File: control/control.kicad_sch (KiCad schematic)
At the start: 51 parts, among them J1 Conn_01x02_Pin, J3 Conn_01x02_Pin, J4 Conn_01x07_Pin, J9 Conn_01x04_Male, P1 Conn_01x03_Pin, P2 Conn_01x03_Pin, P3 Conn_01x03_Pin, P4 Conn_01x03_Pin, SW1 SW_Push, U1 STM32F103C8Tx, Y1 8Mhz

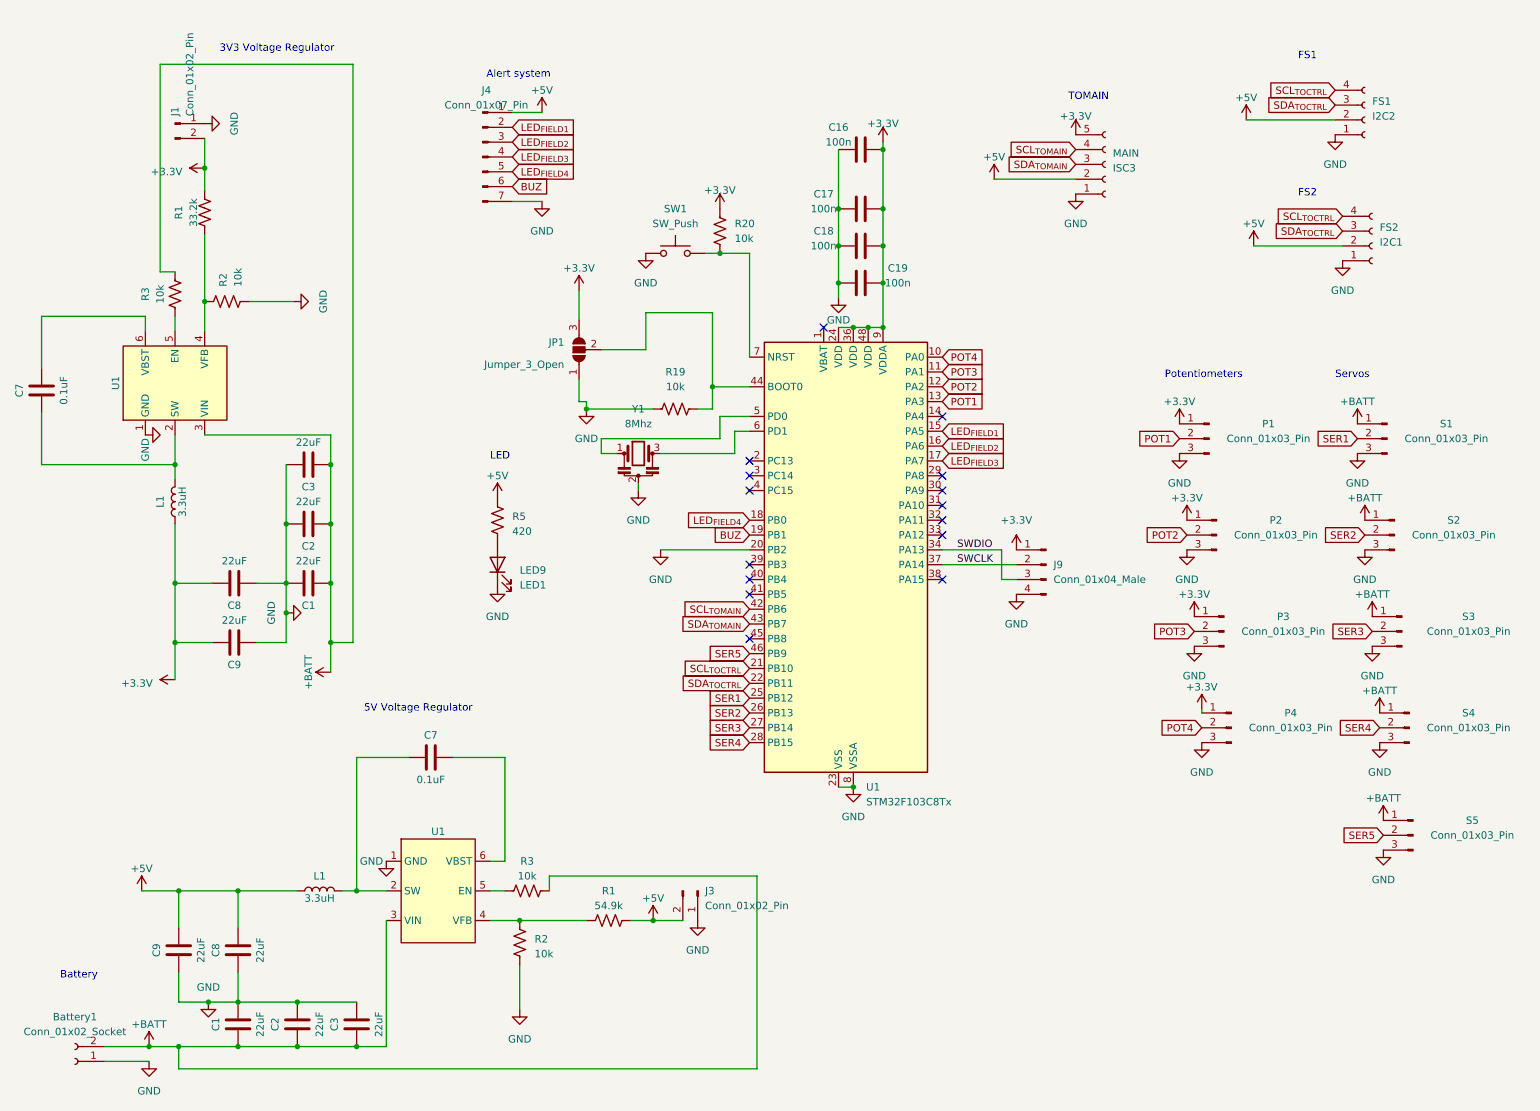
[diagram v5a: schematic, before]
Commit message: increased size and updated silkscreen labels
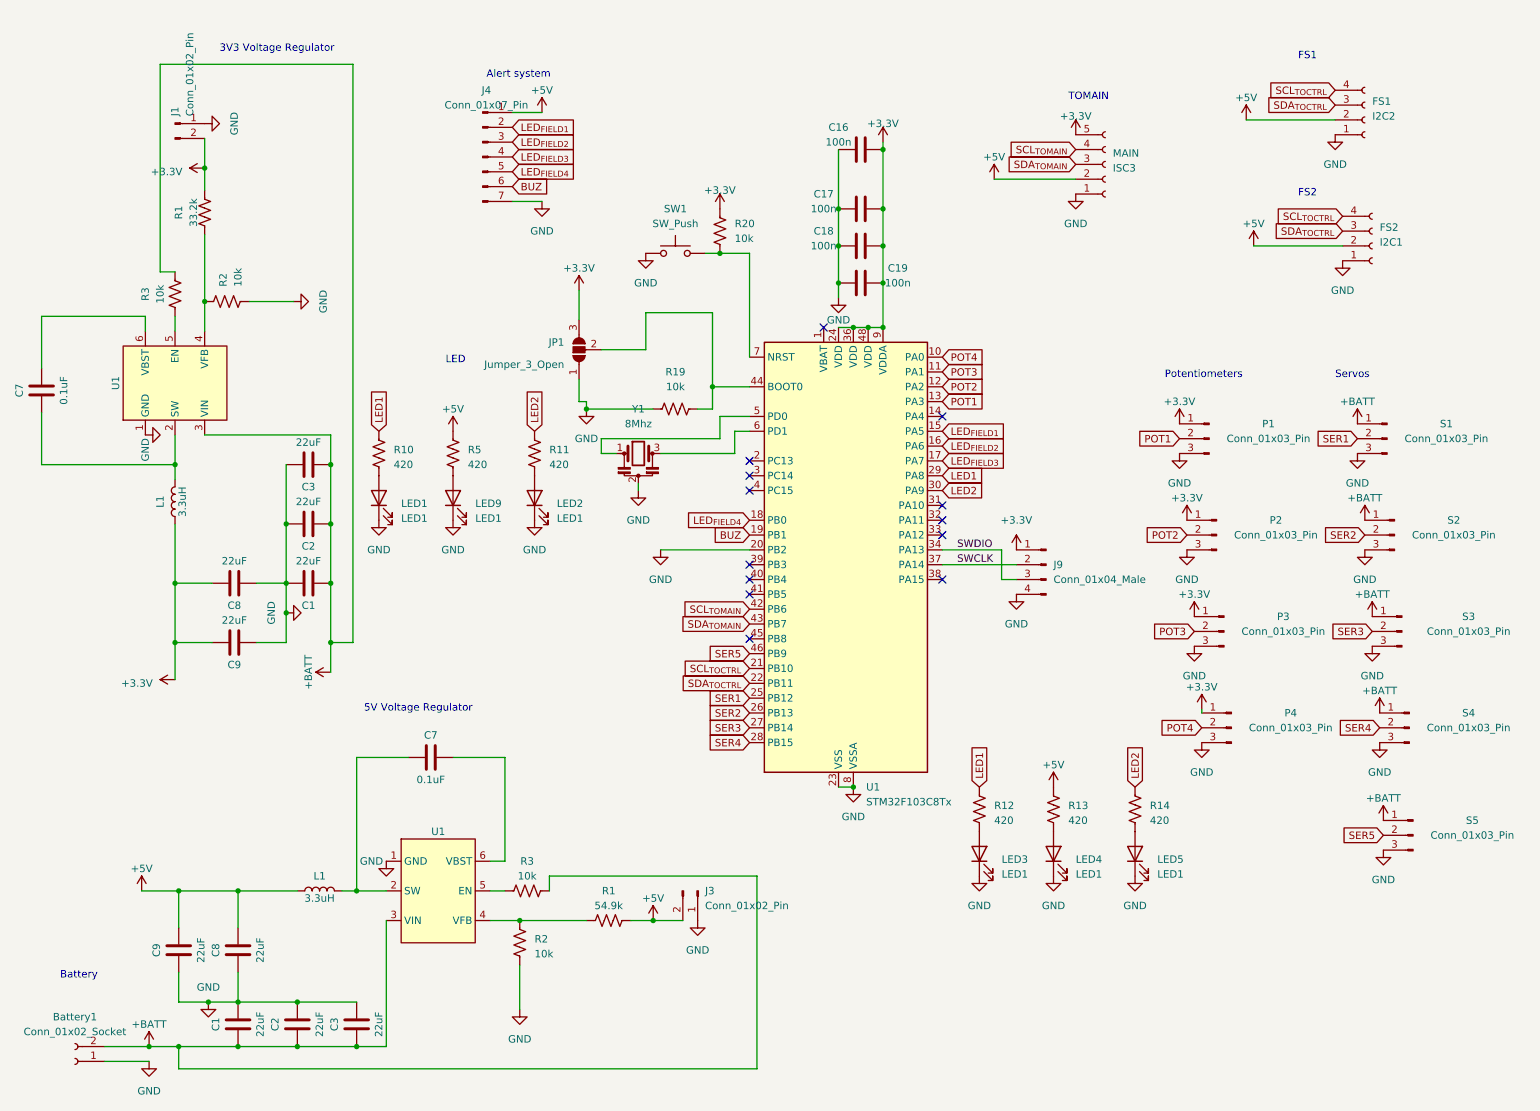
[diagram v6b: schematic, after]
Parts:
- added LED1, LED2, LED3, LED4, LED5: LED1, LED_SMD:LED_0805_2012Metric_Pad1.15x1.40mm_HandSolder, symbol Device:LED
- added R10, R11, R12, R13, R14: 420, Resistor_SMD:R_0603_1608Metric, symbol Device:R_US
- Battery1: footprint Connector_Wire:SolderWire-2sqmm_1x02_P7.8mm_D2mm_OD3.9mm -> Connector_AMASS:AMASS_XT60-F_1x02_P7.20mm_Vertical
- LED9: footprint LED_THT:LED_D4.0mm -> LED_SMD:LED_0805_2012Metric_Pad1.15x1.40mm_HandSolder
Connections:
- net +5V: now also R13.2
- net GND: now also LED1.1 (K), LED2.1 (K), LED3.1 (K), LED4.1 (K), LED5.1 (K)
- net LED1: now reaches U1.29 (PA8)
- net LED1: now also R10.2, R12.2
- net LED2: now reaches U1.30 (PA9)
- net LED2: now also R11.2, R14.2
- new net: LED5.2 (A), R14.1
- new net: LED1.2 (A), R10.1
- new net: LED2.2 (A), R11.1
- new net: LED3.2 (A), R12.1
- new net: LED4.2 (A), R13.1
- no-connect marks 15 -> 13
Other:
- moved on the sheet: LED9, R5

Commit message: updated board shape, added silkscreen labels & new LEDs
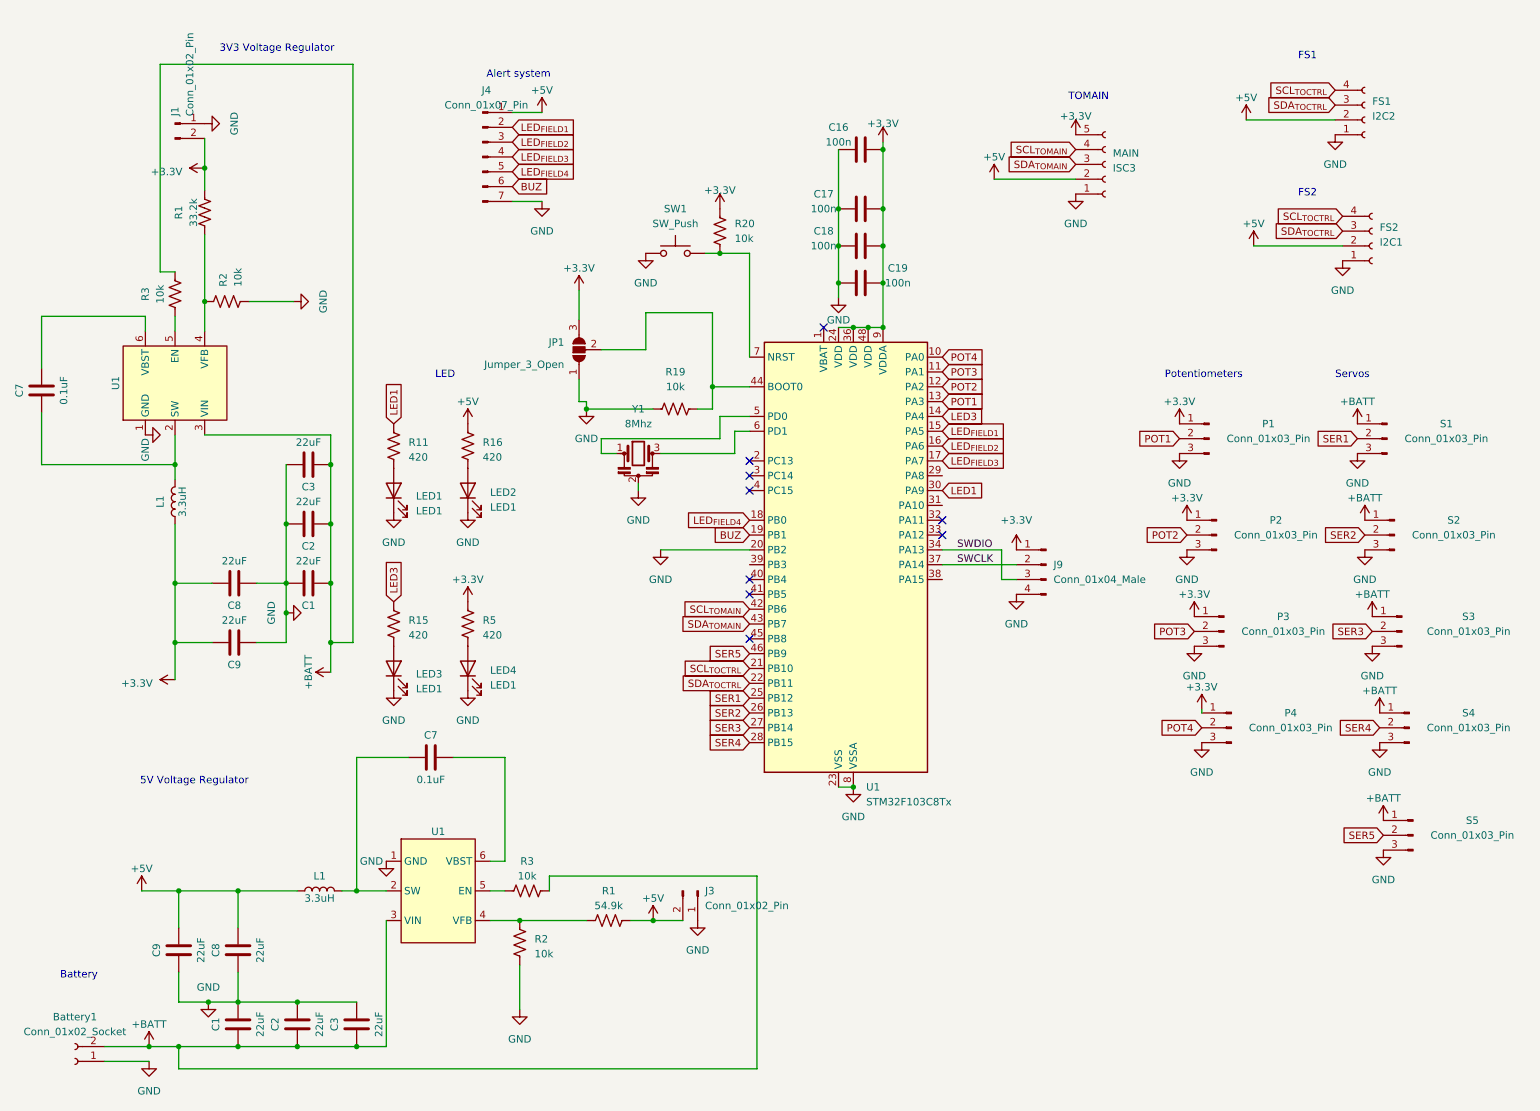
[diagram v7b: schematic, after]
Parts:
- removed LED1, LED4, LED5: LED1, LED_SMD:LED_0805_2012Metric_Pad1.15x1.40mm_HandSolder, symbol Device:LED
- removed R10, R12, R13, R14: 420, Resistor_SMD:R_0603_1608Metric, symbol Device:R_US
- added LED2: LED1, LED_SMD:LED_0805_2012Metric_Pad1.15x1.40mm_HandSolder, symbol Device:LED
- added R15, R16: 420, Resistor_SMD:R_0603_1608Metric, symbol Device:R_US
- renumbered LED2 to LED1, LED9 to LED4
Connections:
- net LED2 is gone; now on net LED1: R11.2, U1.30 (PA9)
- net +3.3V: now also R5.2
- net +5V: now also R16.2; no longer R5.2
- net GND: now also LED2.1 (K)
- net LED1: no longer U1.29 (PA8)
- net at LED3.2 (A): now also R15.1
- net LED3: now reaches U1.14 (PA4)
- net LED3: now also R15.2
- new net: LED2.2 (A), R16.1
- no-connect marks 13 -> 9
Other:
- moved on the sheet: LED1, LED4, R11, R5

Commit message: updated programmer & battery footprints
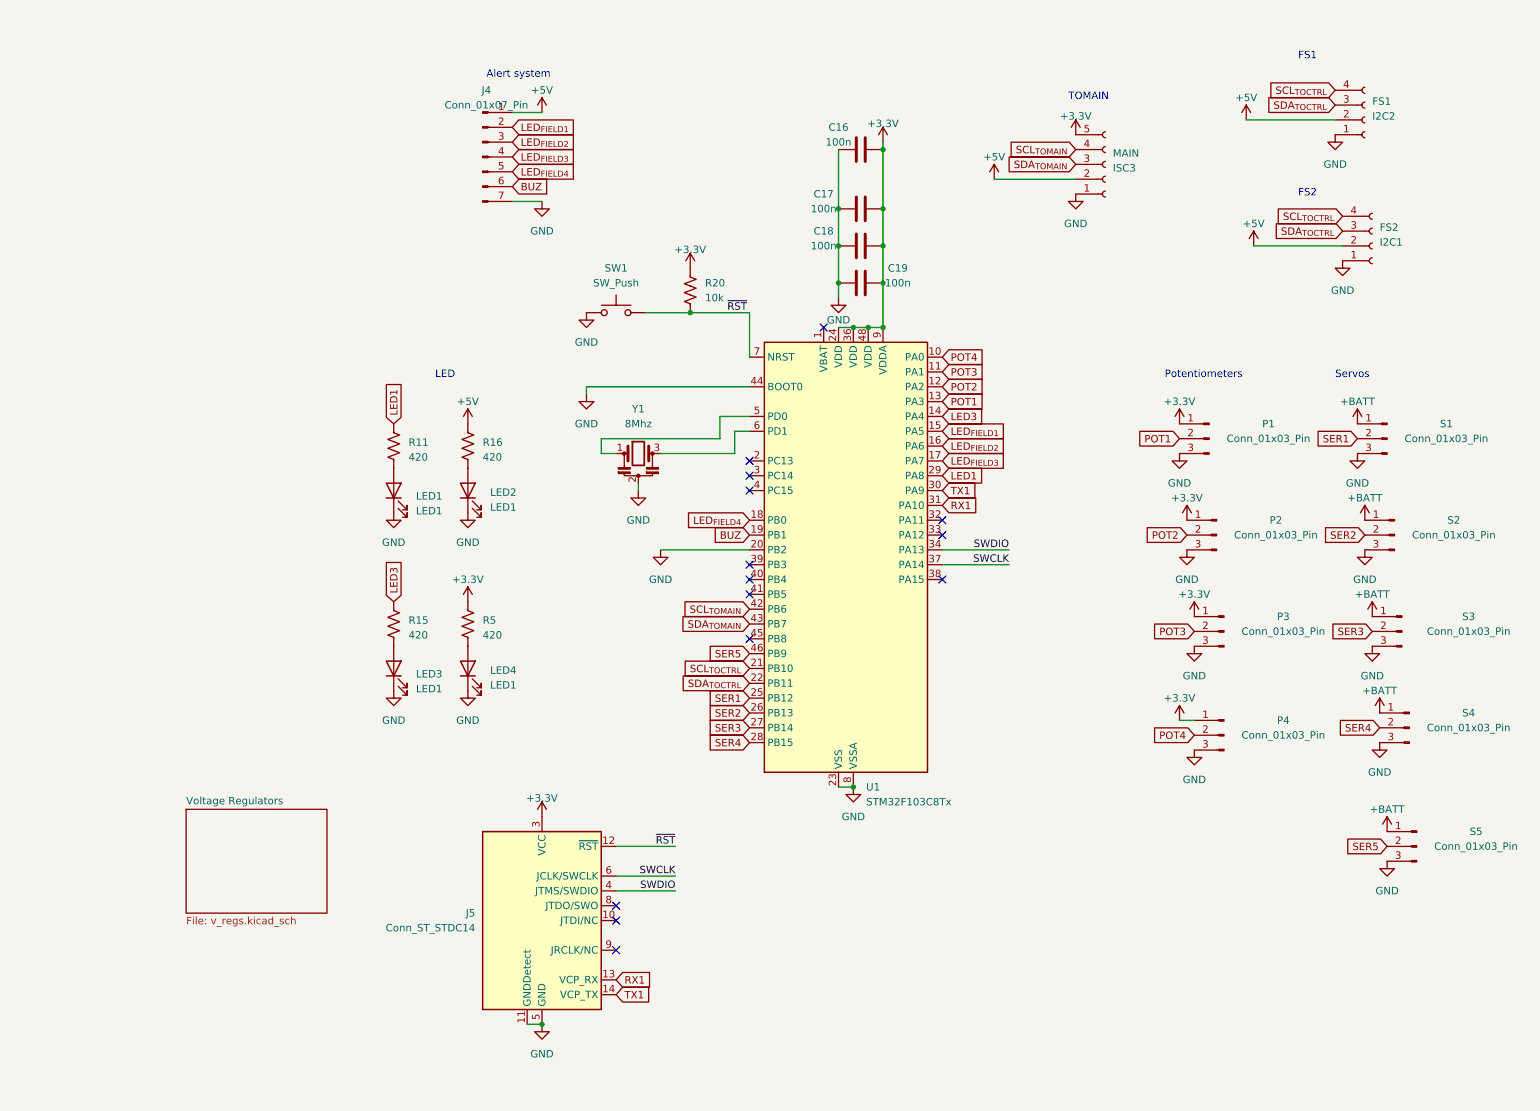
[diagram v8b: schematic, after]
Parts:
- removed Battery1: Conn_01x02_Socket, Connector_AMASS:AMASS_XT60-F_1x02_P7.20mm_Vertical, symbol Connector:Conn_01x02_Socket
- removed C1 (x2), C2 (x2), C3 (x2), C8 (x2), C9 (x2): 22uF, Capacitor_SMD:C_0805_2012Metric, symbol Device:C
- removed C7 (x2): 0.1uF, Capacitor_SMD:C_0805_2012Metric, symbol Device:C
- removed J1, J3: Conn_01x02_Pin, Connector_JST:JST_XH_B2B-XH-A_1x02_P2.50mm_Vertical, symbol Connector:Conn_01x02_Pin
- removed J9: Conn_01x04_Male, Connector_PinHeader_2.54mm:PinHeader_1x04_P2.54mm_Horizontal, symbol Connector:Conn_01x04_Male
- removed JP1: Jumper_3_Open, Jumper:SolderJumper-3_P2.0mm_Open_TrianglePad1.0x1.5mm, symbol Jumper:SolderJumper_3_Open
- removed L1 (x2): 3.3uH, Inductor_SMD:L_Taiyo-Yuden_NR-60xx, symbol Device:L
- removed R1: 33.2k, Resistor_SMD:R_0603_1608Metric, symbol Device:R_US
- removed R1: 54.9k, Resistor_SMD:R_0603_1608Metric, symbol Device:R_US
- removed R19, R2 (x2), R3 (x2): 10k, Resistor_SMD:R_0603_1608Metric, symbol Device:R_US
- removed U1 (x2): ~, Package_TO_SOT_SMD:TSOT-23-6, symbol Regulators:TPS563208DDCR
- added J5: Conn_ST_STDC14, Connector_PinHeader_1.27mm:PinHeader_2x07_P1.27mm_Vertical_SMD, symbol Connector:Conn_ST_STDC14
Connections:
- net +3.3V: now also J5.3 (VCC)
- net GND: now also U1.44 (BOOT0), J5.11 (GNDDetect), J5.5 (GND), J5.7 (GND)
- net LED1: now also U1.29 (PA8); no longer U1.30 (PA9)
- net SWCLK: now also J5.6 (JCLK/SWCLK)
- net SWDIO: now also J5.4 (JTMS/SWDIO)
- net ~{RST}: now reaches R20.2, SW1.2, U1.7 (NRST)
- net ~{RST}: now also J5.12 (~{RST})
- net RX1: now reaches U1.31 (PA10)
- net RX1: now also J5.13 (VCP_RX)
- new net TX1: J5.14 (VCP_TX), U1.30 (PA9)
- no-connect marks 9 -> 14
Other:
- added sheet Voltage Regulators (v_regs.kicad_sch)
- note removed: "3V3 Voltage Regulator"
- note removed: "5V Voltage Regulator"
- note removed: "Battery"
- moved on the sheet: P4, R20, S5, SW1
